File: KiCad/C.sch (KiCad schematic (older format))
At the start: 5 parts

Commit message: update schematics and libraries
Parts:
- gave numbers to parts that had none: 5
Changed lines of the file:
@@
 P 5650 4050
 AR Path="/6178215D/61782184/6178B22C" Ref="U?"  Part="1"
-AR Path="/6178215D/6178A189/6178B22C" Ref="U?"  Part="1"
-F 0 "U?" H 5750 4200 50  0000 L CNN
+AR Path="/6178215D/6178A189/6178B22C" Ref="U3"  Part="1"
+F 0 "U3" H 5750 4200 50  0000 L CNN
 F 1 "OPAMP" H 5994 4005 50  0001 L CNN
 F 2 "" H 5650 4050 50  0001 C CNN
@@
 P 5550 3600
 AR Path="/6178215D/61782184/6178B233" Ref="#PWR?"  Part="1"
-AR Path="/6178215D/6178A189/6178B233" Ref="#PWR?"  Part="1"
-F 0 "#PWR?" H 5550 3450 50  0001 C CNN
+AR Path="/6178215D/6178A189/6178B233" Ref="#PWR09"  Part="1"
+F 0 "#PWR09" H 5550 3450 50  0001 C CNN
 F 1 "VCC" H 5567 3773 50  0000 C CNN
 F 2 "" H 5550 3600 50  0001 C CNN
@@
 P 5550 4450
 AR Path="/6178215D/61782184/6178B23A" Ref="#PWR?"  Part="1"
-AR Path="/6178215D/6178A189/6178B23A" Ref="#PWR?"  Part="1"
-F 0 "#PWR?" H 5550 4200 50  0001 C CNN
+AR Path="/6178215D/6178A189/6178B23A" Ref="#PWR010"  Part="1"
+F 0 "#PWR010" H 5550 4200 50  0001 C CNN
 F 1 "GND" H 5555 4277 50  0000 C CNN
 F 2 "" H 5550 4450 50  0001 C CNN
@@
 P 5100 3500
 AR Path="/6178215D/61782184/6178B242" Ref="Rb?"  Part="1"
-AR Path="/6178215D/6178A189/6178B242" Ref="Rb?"  Part="1"
-F 0 "Rb?" H 5170 3500 50  0000 L CNN
+AR Path="/6178215D/6178A189/6178B242" Ref="Rb5"  Part="1"
+F 0 "Rb5" H 5170 3500 50  0000 L CNN
 F 1 "R" H 5170 3455 50  0001 L CNN
 F 2 "" V 5030 3500 50  0001 C CNN
@@
 P 4700 3950
 AR Path="/6178215D/61782184/6178B24B" Ref="Ra?"  Part="1"
-AR Path="/6178215D/6178A189/6178B24B" Ref="Ra?"  Part="1"
-F 0 "Ra?" V 4585 3950 50  0000 C CNN
+AR Path="/6178215D/6178A189/6178B24B" Ref="Ra5"  Part="1"
+F 0 "Ra5" V 4585 3950 50  0000 C CNN
 F 1 "R" V 4584 3950 50  0001 C CNN
 F 2 "" V 4630 3950 50  0001 C CNN
@@
 P 4700 4150
 AR Path="/6178215D/61782184/6178B255" Ref="Ra?"  Part="1"
-AR Path="/6178215D/6178A189/6178B255" Ref="Ra?"  Part="1"
-F 0 "Ra?" V 4585 4150 50  0000 C CNN
+AR Path="/6178215D/6178A189/6178B255" Ref="Ra6"  Part="1"
+F 0 "Ra6" V 4585 4150 50  0000 C CNN
 F 1 "R" V 4584 4150 50  0001 C CNN
 F 2 "" V 4630 4150 50  0001 C CNN
@@
 P 5900 4700
 AR Path="/6178215D/61782184/6178B260" Ref="Rb?"  Part="1"
-AR Path="/6178215D/6178A189/6178B260" Ref="Rb?"  Part="1"
-F 0 "Rb?" V 5785 4700 50  0000 C CNN
+AR Path="/6178215D/6178A189/6178B260" Ref="Rb6"  Part="1"
+F 0 "Rb6" V 5785 4700 50  0000 C CNN
 F 1 "R" V 5784 4700 50  0001 C CNN
 F 2 "" V 5830 4700 50  0001 C CNN

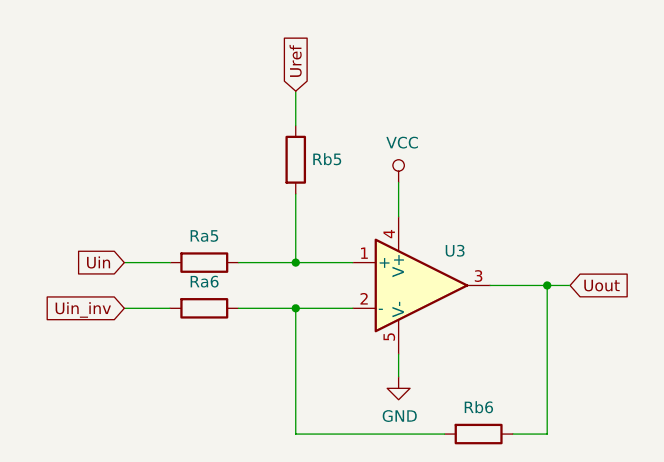
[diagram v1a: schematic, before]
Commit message: corrected opamp circuits
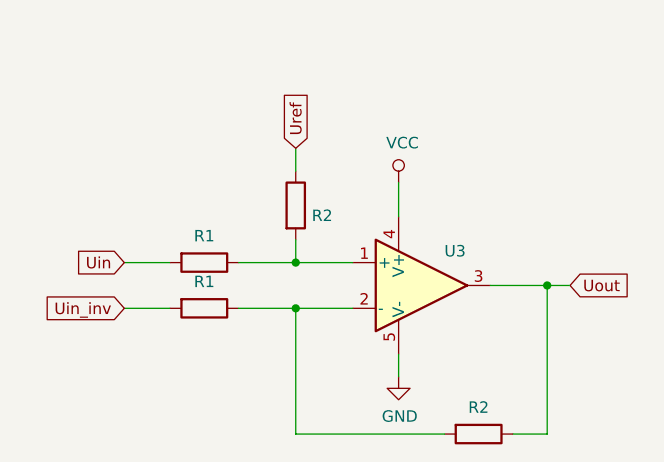
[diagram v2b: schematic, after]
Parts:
- R2: renamed from Rb6; value R -> R2
- Ra5, Ra6: value R -> R1
- Rb5: value R -> R2
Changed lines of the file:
@@
 	5350 3950 5100 3950
 Wire Wire Line
-	5100 3950 5100 3650
+	5100 3950 5100 3850
 $Comp
 L Device:R Rb?
 U 1 1 6178B242
-P 5100 3500
+P 5100 3700
 AR Path="/6178215D/61782184/6178B242" Ref="Rb?"  Part="1"
 AR Path="/6178215D/6178A189/6178B242" Ref="Rb5"  Part="1"
-F 0 "Rb5" H 5170 3500 50  0000 L CNN
-F 1 "R" H 5170 3455 50  0001 L CNN
-F 2 "" V 5030 3500 50  0001 C CNN
-F 3 "~" H 5100 3500 50  0001 C CNN
-	1    5100 3500
+F 0 "Rb5" H 5170 3700 50  0001 L CNN
+F 1 "R2" H 5170 3655 50  0000 L CNN
+F 2 "" V 5030 3700 50  0001 C CNN
+F 3 "~" H 5100 3700 50  0001 C CNN
+	1    5100 3700
 	1    0    0    -1
 $EndComp
 Wire Wire Line
-	5100 3350 5100 3200
+	5100 3550 5100 3450
 Wire Wire Line
 	5100 3950 4850 3950
@@
 AR Path="/6178215D/61782184/6178B24B" Ref="Ra?"  Part="1"
 AR Path="/6178215D/6178A189/6178B24B" Ref="Ra5"  Part="1"
-F 0 "Ra5" V 4585 3950 50  0000 C CNN
-F 1 "R" V 4584 3950 50  0001 C CNN
+F 0 "Ra5" V 4585 3950 50  0001 C CNN
+F 1 "R1" V 4584 3950 50  0000 C CNN
 F 2 "" V 4630 3950 50  0001 C CNN
 F 3 "~" H 4700 3950 50  0001 C CNN
@@
 AR Path="/6178215D/61782184/6178B255" Ref="Ra?"  Part="1"
 AR Path="/6178215D/6178A189/6178B255" Ref="Ra6"  Part="1"
-F 0 "Ra6" V 4585 4150 50  0000 C CNN
-F 1 "R" V 4584 4150 50  0001 C CNN
+F 0 "Ra6" V 4585 4150 50  0001 C CNN
+F 1 "R1" V 4584 4150 50  0000 C CNN
 F 2 "" V 4630 4150 50  0001 C CNN
 F 3 "~" H 4700 4150 50  0001 C CNN
@@
 P 5900 4700
 AR Path="/6178215D/61782184/6178B260" Ref="Rb?"  Part="1"
-AR Path="/6178215D/6178A189/6178B260" Ref="Rb6"  Part="1"
-F 0 "Rb6" V 5785 4700 50  0000 C CNN
-F 1 "R" V 5784 4700 50  0001 C CNN
+AR Path="/6178215D/6178A189/6178B260" Ref="R2"  Part="1"
+F 0 "R2" V 5785 4700 50  0001 C CNN
+F 1 "R2" V 5784 4700 50  0000 C CNN
 F 2 "" V 5830 4700 50  0001 C CNN
 F 3 "~" H 5900 4700 50  0001 C CNN
@@
 Wire Wire Line
 	6200 4050 5950 4050
-Text GLabel 5100 3200 1    50   Input ~ 0
+Text GLabel 5100 3450 1    50   Input ~ 0
 Uref
 Wire Wire Line
